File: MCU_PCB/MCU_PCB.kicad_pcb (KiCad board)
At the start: 2 copper layers, 70 x 70 mm, 5 parts, among them J1 BackBone, J2 D1, J3 D2

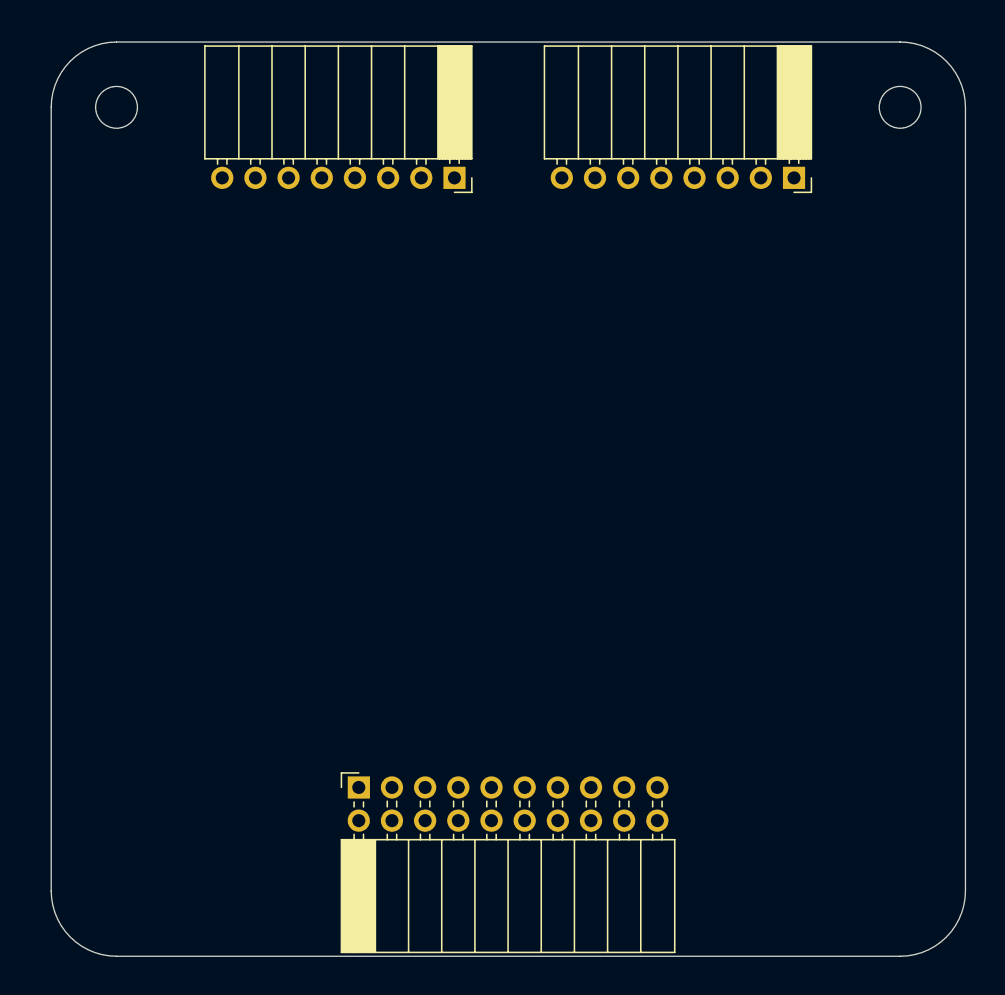
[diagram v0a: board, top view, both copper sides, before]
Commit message: 0.1v MCU KiCad
Aesthetics needs to be improved.
Trace width needs to be changed.
More sufficient grounding.
Component placement could be changed.
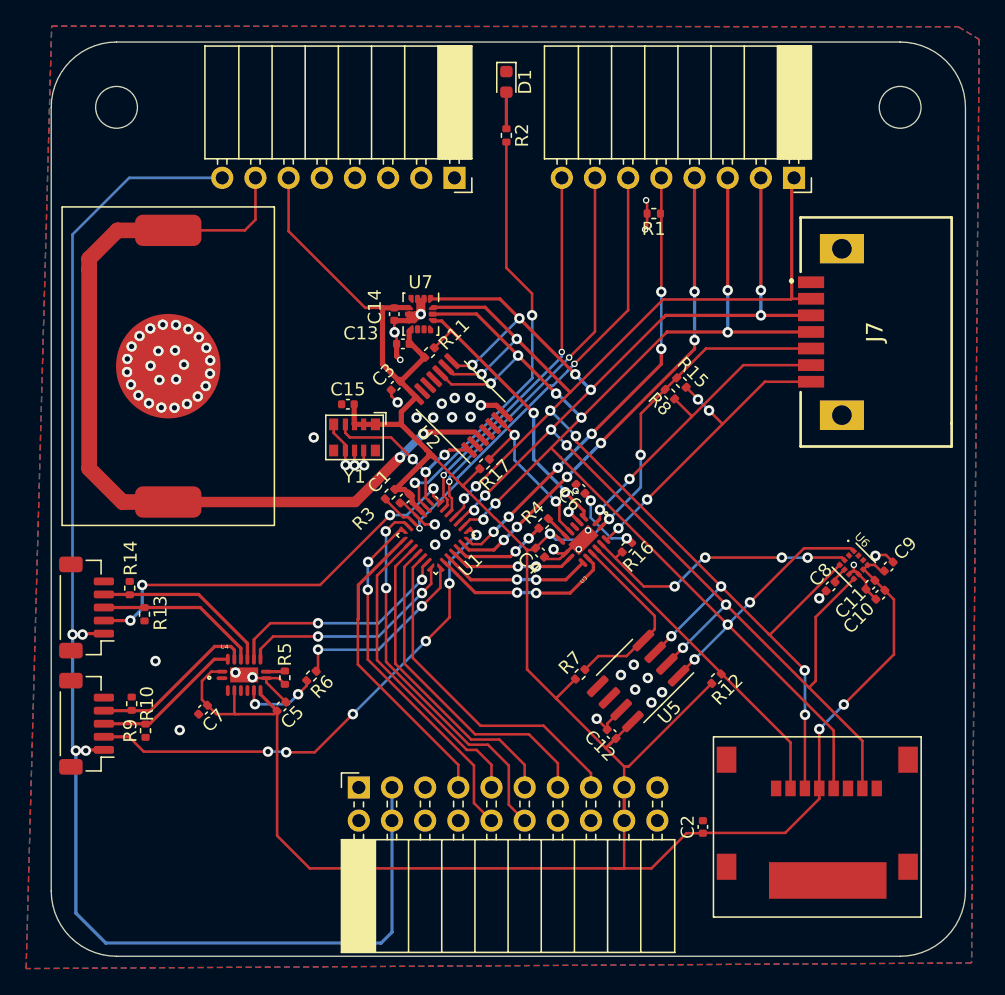
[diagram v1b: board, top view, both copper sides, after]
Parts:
- added BT1: 3.3V, footprints:3034, F.Cu at (101.6, 88.4)
- added C1: 100nF, Capacitor_SMD:C_0402_1005Metric, F.Cu at (119.7, 98.6)
- added C10: 10uF, Capacitor_SMD:C_0402_1005Metric, F.Cu at (156.1, 105.9)
- added C11: 100nF, Capacitor_SMD:C_0402_1005Metric, F.Cu at (155.3, 105.2)
- added C12: 100nF, Capacitor_SMD:C_0402_1005Metric, F.Cu at (135.5, 116.6)
- added C13: 100nF, Capacitor_SMD:C_0402_1005Metric, F.Cu at (119.5, 86.7)
- added C14: 100nF, Capacitor_SMD:C_0402_1005Metric, F.Cu at (118.9, 84.4)
- added C15: 100nF, Capacitor_SMD:C_0402_1005Metric, F.Cu at (115.3, 91.3)
- added C2: 100nF, Capacitor_SMD:C_0402_1005Metric, F.Cu at (142.5, 123.7)
- added C3: 100nF, Capacitor_SMD:C_0402_1005Metric, F.Cu at (119.0, 89.9)
- added C4: 100nF, Capacitor_SMD:C_0402_1005Metric, F.Cu at (130.0, 102.7)
- added C5: 100nF, Capacitor_SMD:C_0402_1005Metric, F.Cu at (110.2, 114.5)
- added C6: 100nF, Capacitor_SMD:C_0402_1005Metric, F.Cu at (133.1, 97.8)
- added C7: 100nF, Capacitor_SMD:C_0402_1005Metric, F.Cu at (104.2, 114.7)
- added C8: 220nF, Capacitor_SMD:C_0402_1005Metric, F.Cu at (152.3, 105.3)
- added C9: 100nF, Capacitor_SMD:C_0402_1005Metric, F.Cu at (156.7, 103.8)
- added D1: LED, LED_SMD:LED_0603_1608Metric, F.Cu at (127.5, 66.7)
- added J4: Micro_SD_Card, footprints:Micro_SD, F.Cu at (153.8, 122.6)
- added J5: CAM_0, Connector_JST:JST_SH_BM05B-SRSS-TB_1x05-1MP_P1.00mm_Vertical, F.Cu at (95.3, 115.8)
- added J6: CAM_1, Connector_JST:JST_SH_BM05B-SRSS-TB_1x05-1MP_P1.00mm_Vertical, F.Cu at (95.3, 106.9)
- added J7: 47080-4005, footprints:470804005, F.Cu at (155.7, 85.8)
- added R1: 12k, Resistor_SMD:R_0402_1005Metric, F.Cu at (138.7, 76.7)
- added R10: 12k, Resistor_SMD:R_0402_1005Metric, F.Cu at (98.8, 114.3)
- added R11: 12k, Resistor_SMD:R_0402_1005Metric, F.Cu at (121.6, 87.4)
- added R12: 12k, Resistor_SMD:R_0402_1005Metric, F.Cu at (143.5, 112.3)
- added R13: 12k, Resistor_SMD:R_0402_1005Metric, F.Cu at (99.7, 107.4)
- added R14: 12k, Resistor_SMD:R_0402_1005Metric, F.Cu at (98.6, 105.4)
- added R15: 12k, Resistor_SMD:R_0402_1005Metric, F.Cu at (140.9, 89.7)
- added R16: 12k, Resistor_SMD:R_0402_1005Metric, F.Cu at (136.7, 102.3)
- added R17: 12k, Resistor_SMD:R_0402_1005Metric, F.Cu at (125.8, 95.9)
- added R2: 330, Resistor_SMD:R_0402_1005Metric, F.Cu at (127.5, 70.8)
- added R3: 12k, Resistor_SMD:R_0402_1005Metric, F.Cu at (118.5, 98.2)
- added R4: 12k, Resistor_SMD:R_0402_1005Metric, F.Cu at (130.3, 100.5)
- added R5: 12k, Resistor_SMD:R_0402_1005Metric, F.Cu at (110.5, 112.3)
- added R6: 12k, Resistor_SMD:R_0402_1005Metric, F.Cu at (112.5, 112.1)
- added R7: 12k, Resistor_SMD:R_0402_1005Metric, F.Cu at (133.1, 112.0)
- added R8: 12k, Resistor_SMD:R_0402_1005Metric, F.Cu at (140.0, 90.6)
- added R9: 12k, Resistor_SMD:R_0402_1005Metric, F.Cu at (99.8, 116.3)
- added U1: STM32G071GBU, Package_DFN_QFN:QFN-28_4x4mm_P0.5mm, F.Cu at (122.0, 101.4)
- added U2: MCP795W22-I/ST, Package_SO:TSSOP-14_4.4x5mm_P0.65mm, F.Cu at (124.0, 91.4)
- added U3: 74HCT4051BQ-Q100,1, footprints:QFN50P250X350X100-17N, F.Cu at (133.3, 101.7)
- added U4: 74HCT4051BQ-Q100,1, footprints:QFN50P250X350X100-17N, F.Cu at (107.4, 112.1)
- added U5: ADT7310, Package_SO:SOIC-8_3.9x4.9mm_P1.27mm, F.Cu at (137.5, 112.5)
- added U6: LIS2MDLTR, footprints:PQFN50P200X200X70-12N, F.Cu at (154.1, 103.6)
- added U7: LSM6DSRX, Package_LGA:LGA-14_3x2.5mm_P0.5mm_LayoutBorder3x4y, F.Cu at (120.9, 84.4)
- added Y1: TG-3541CE, footprints:Oscillator_SMD_SeikoEpson_TG-3541CE_3.2x2.5mm, F.Cu at (115.8, 93.9)
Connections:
- J1 pad 10: unconnected-(J1-Pad10) -> /IO/COM_RX
- J1 pad 11: unconnected-(J1-Pad11) -> /IO/ADC_4V
- J1 pad 12: unconnected-(J1-Pad12) -> /IO/COM_TX
- J1 pad 13: unconnected-(J1-Pad13) -> /IO/ROPE_CUT
- J1 pad 15: unconnected-(J1-Pad15) -> /IO/BUZZER
- J1 pad 7: unconnected-(J1-Pad7) -> /IO/ADC_VBAT
- J1 pad 9: unconnected-(J1-Pad9) -> /IO/ADC_3.3V
- J2 pad 3: unconnected-(J2-Pad3) -> GND
- J2 pad 4: unconnected-(J2-Pad4) -> GND
- J2 pad 5: unconnected-(J2-Pad5) -> GND
- J2 pad 6: unconnected-(J2-Pad6) -> +3V3
- J2 pad 7: unconnected-(J2-Pad7) -> +BATT
- J2 pad 8: unconnected-(J2-Pad8) -> +4V
- J3 pad 1: unconnected-(J3-Pad1) -> /CAM_SENS/MOSI
- J3 pad 2: unconnected-(J3-Pad2) -> /CAM_SENS/MISO
- J3 pad 3: unconnected-(J3-Pad3) -> /CAM_SENS/CLK
- J3 pad 4: unconnected-(J3-Pad4) -> /IO/SW_IO
- J3 pad 5: unconnected-(J3-Pad5) -> /IO/SW_CLK
- J3 pad 6: unconnected-(J3-Pad6) -> /IO/~{RST}
- J3 pad 7: GND -> /IO/TX
- J3 pad 8: GND -> /IO/RX
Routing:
- net +3V3: track 0.00 -> 234.2 mm, vias 0 -> 7
- net /CAM_SENS/MISO: track 0.00 -> 119.7 mm, vias 0 -> 12
- net /CAM_SENS/CLK: track 0.00 -> 119.5 mm, vias 0 -> 11
- net /CAM_SENS/MOSI: track 0.00 -> 115.9 mm, vias 0 -> 10
- net +4V: track 0.00 -> 107.3 mm, vias 0 -> 4
- net +BATT: track 0.00 -> 74.6 mm, vias 0 -> 2
- net GND: track 0.00 -> 50.9 mm, vias 0 -> 66
- net /CAM_SENS/HB_0: track 0.00 -> 39.2 mm, vias 0 -> 6
- net /IO/SW_IO: track 0.00 -> 37.4 mm, vias 0 -> 6
- net /IO/~{RST}: track 0.00 -> 36.9 mm, vias 0 -> 2
- net /IO/SW_CLK: track 0.00 -> 34.9 mm, vias 0 -> 6
- net /MCU/LED_0: track 0.00 -> 33.5 mm, vias 0 -> 2
- net /CAM_SENS/HB_1: track 0.00 -> 31.8 mm, vias 0 -> 4
- net /IO/TX: track 0.00 -> 30.4 mm, vias 0 -> 2
- net /IO/COM_TX: track 0.00 -> 29.6 mm, vias 0 -> 2
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- added copper zone on B.Cu, net GND
- added copper zone on F.Cu, net GND
